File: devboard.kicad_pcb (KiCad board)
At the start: 2 copper layers, 23 x 55.5 mm, 29 parts, among them J1 USB4105-GF-A, J2 Conn_01x08_Pin, J3 Conn_01x08_Pin, U1 STM32F411CEU6, U2 AP2120N-3.3TRG1, U3 USBLC6-2SC6Y

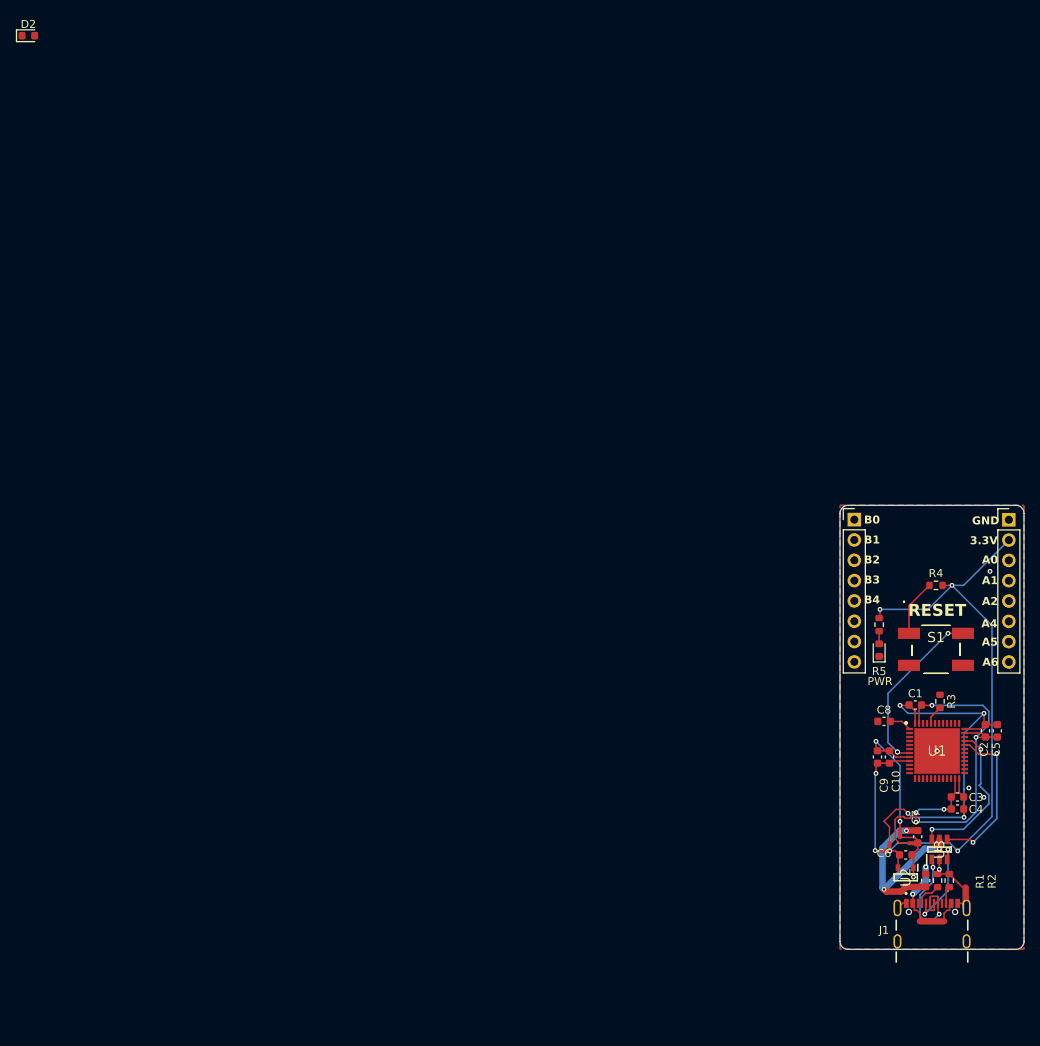
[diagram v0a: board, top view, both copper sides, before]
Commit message: Total board refactoring: - Full board routing - Ready for manufacturing - Schematic fixing ad improvements
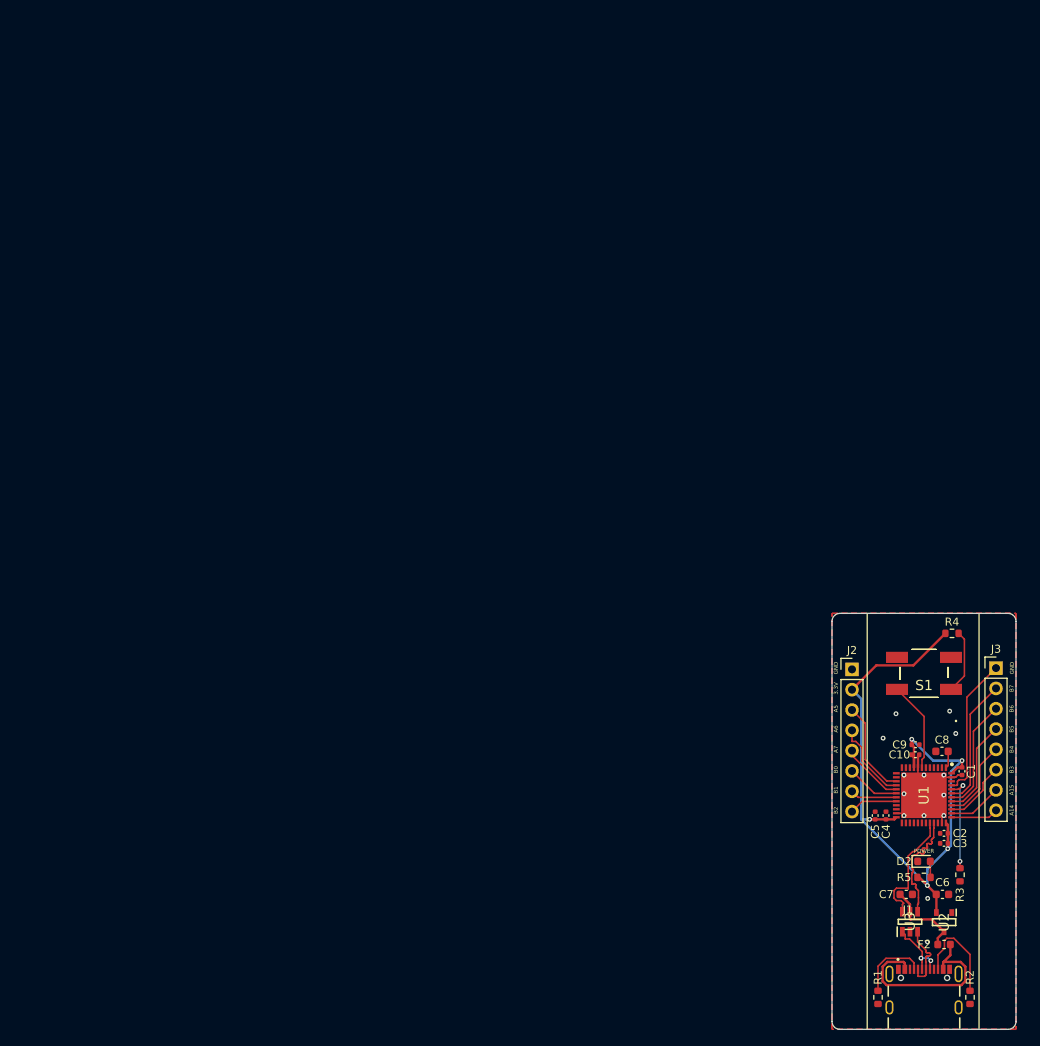
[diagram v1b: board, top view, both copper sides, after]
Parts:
- removed NT1, NT2, NT3, NT4: NetTie_2, NetTie:NetTie-2_SMD_Pad0.5mm
- removed PWR: LED, LED_SMD:LED_0603_1608Metric
- C1, C10, C2, C3, C4, C5, C9: footprint Capacitor_SMD:C_0603_1608Metric -> Capacitor_SMD:C_0402_1005Metric
- moved D2 152.3 mm to (113.5, 104.0)
- moved R5 32.1 mm to (113.5, 106.0), turned to 180 degrees
- moved J2 27.1 mm to (104.5, 80.0)
- moved J3 25.7 mm to (122.5, 79.8)
- moved R3 21.8 mm to (118.0, 105.7), turned to 90 degrees
- moved C5 18.6 mm to (107.4, 98.3), turned to 90 degrees
- moved R1 16.4 mm to (107.8, 121.0), turned to -90 degrees
- moved R2 14.8 mm to (119.2, 121.0), turned to -90 degrees
- moved C2 13.8 mm to (116.0, 100.5), turned to 180 degrees
- moved C1 10.1 mm to (118.2, 92.7), turned to -90 degrees
- moved U3 9.76 mm to (111.8, 111.5)
- moved C4 8.97 mm to (108.8, 98.3), turned to 90 degrees
- moved F2 8.32 mm to (116.0, 114.4), turned to 0 degrees
- moved J1 8.31 mm to (113.5, 122.2)
- moved C8 8.16 mm to (115.8, 90.2)
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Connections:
- C1 pad 1: Decoupling3.3V -> +3.3V
- C1 pad 2: DecouplingGND -> GND
- C10 pad 1: DecouplingA3.3V -> +3.3V
- C10 pad 2: DecouplingAGND -> GND
- C2 pad 1: Decoupling3.3V -> +3.3V
- C2 pad 2: DecouplingGND -> GND
- C3 pad 1: Decoupling3.3V -> +3.3V
- C3 pad 2: DecouplingGND -> GND
- C4 pad 1: Decoupling3.3V -> +3.3V
- C4 pad 2: DecouplingGND -> GND
- C5 pad 1: Decoupling3.3V -> +3.3V
- C5 pad 2: DecouplingGND -> GND
- C9 pad 1: DecouplingA3.3V -> +3.3V
- C9 pad 2: DecouplingAGND -> GND
- J2 pad 3: A0 -> A5
- J2 pad 4: A1 -> A6
- J2 pad 5: A2 -> A7
- J2 pad 6: A3 -> B0
- J2 pad 7: A4 -> B1
- J2 pad 8: A5 -> B2
- J3 pad 1: B0 -> B8
- J3 pad 2: B1 -> B7
- J3 pad 3: B2 -> B6
- J3 pad 4: B3 -> B5
- J3 pad 6: B5 -> B3
- J3 pad 7: B6 -> A15
- J3 pad 8: B7 -> A14
- U1 pad 23: DecouplingGND -> GND
- U1 pad 24: Decoupling3.3V -> +3.3V
- U1 pad 32: A11 -> USB-
- U1 pad 33: A12 -> USB+
- U1 pad 35: DecouplingGND -> GND
- U1 pad 36: Decoupling3.3V -> +3.3V
- U1 pad 47: DecouplingGND -> GND
- U1 pad 48: Decoupling3.3V -> +3.3V
- U1 pad 8: DecouplingAGND -> GND
- U1 pad 9: DecouplingA3.3V -> +3.3V
- U3 pad 4: A11 -> USB+
- U3 pad 6: A12 -> USB-
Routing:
- net DecouplingGND: track 55.2 -> 0.00 mm, vias 5 -> 0
- net Decoupling3.3V: track 54.1 -> 0.00 mm, vias 4 -> 0
- net A11: track 20.3 -> 0.00 mm, vias 2 -> 0
- net A12: track 19.5 -> 0.00 mm, vias 2 -> 0
- net DecouplingAGND: track 17.8 -> 0.00 mm, vias 2 -> 0
- net +3.3V: track 71.5 -> 89.2 mm, vias 4 -> 5
- net B8: track 0.00 -> 17.8 mm
- net B7: track 0.00 -> 16.2 mm
- net DecouplingA3.3V: track 16.1 -> 0.00 mm, vias 2 -> 0
- net +5V: track 26.3 -> 10.4 mm, vias 3 -> 0
- net USB-: track 0.00 -> 15.0 mm
- net USB+: track 0.00 -> 14.9 mm
- net B6: track 0.00 -> 14.2 mm
- net B5: track 0.00 -> 12.2 mm
- net A5: track 0.00 -> 11.9 mm
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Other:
- board size 23 x 55.5 mm -> 23 x 52 mm
- board text added: "A14"
- board text added: "A15"
- board text added: "A7"
- board text added: "B5"
- board text added: "B6"
- board text added: "B7"
- board text added: "POWER"
- board text removed: "A0"
- board text removed: "A1"
- board text removed: "A2"
- board text removed: "A4"
- board text removed: "RESET"

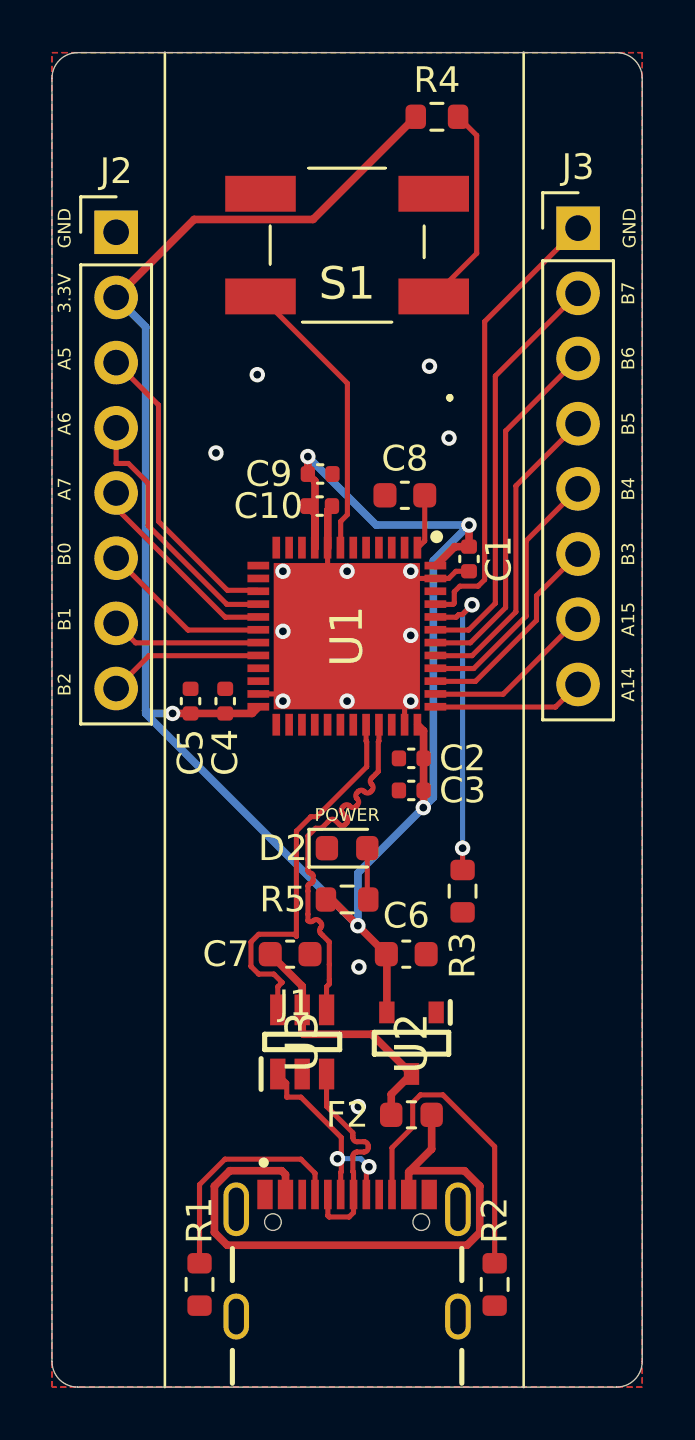
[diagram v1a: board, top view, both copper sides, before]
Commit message: Fixed all DRC errors
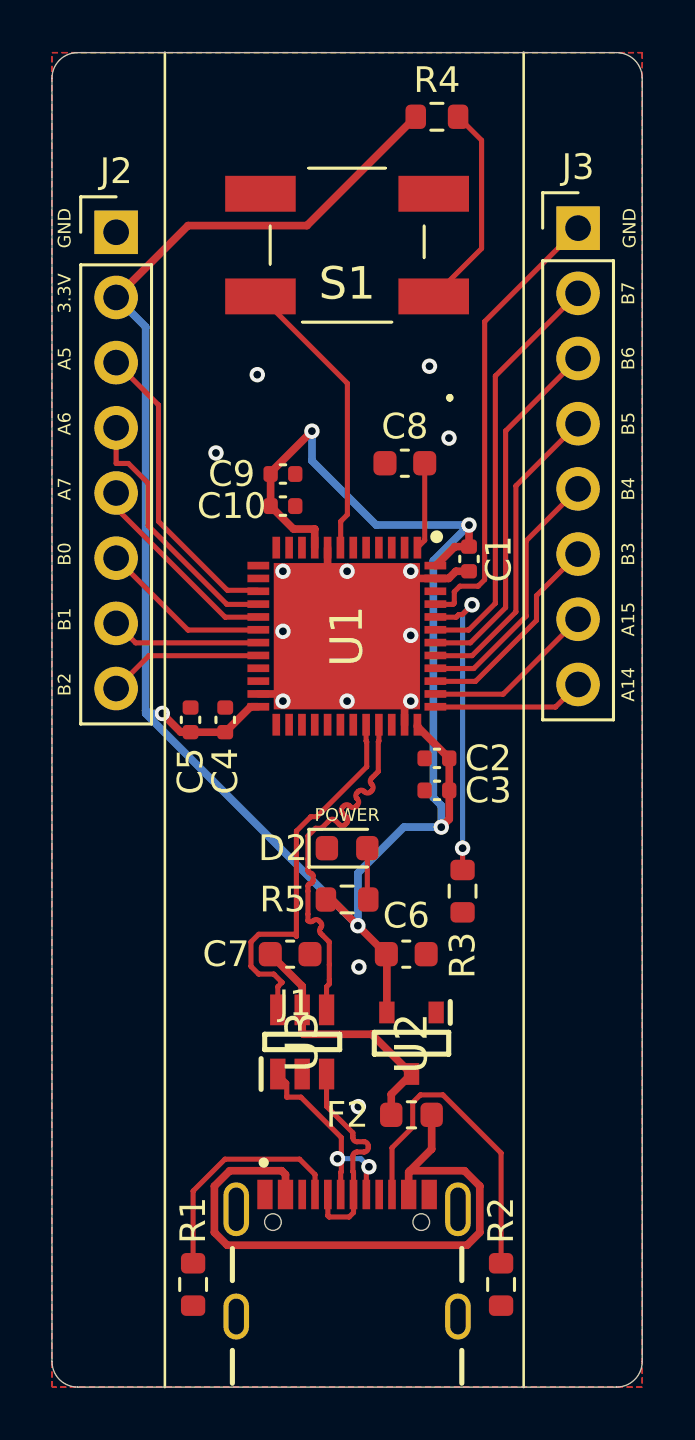
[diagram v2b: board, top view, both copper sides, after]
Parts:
- moved C9 1.45 mm to (111.0, 89.4)
- moved C10 1.43 mm to (111.0, 90.7)
- moved C8 1.25 mm to (115.8, 89.0)
- moved C2 1.00 mm to (117.0, 100.5)
- moved C3 1.00 mm to (117.0, 101.8)
- moved C4 0.73 mm to (108.8, 99.0)
- moved C5 0.73 mm to (107.4, 99.0)
- moved R1 0.25 mm to (107.5, 121.0)
- moved R2 0.25 mm to (119.5, 121.0)
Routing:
- net +3.3V: track 89.2 -> 94.1 mm
- net GND: track 20.0 -> 18.3 mm
- net Net-(U1-VBAT): track 2.16 -> 3.41 mm
